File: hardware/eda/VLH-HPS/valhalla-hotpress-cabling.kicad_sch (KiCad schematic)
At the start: 42 parts

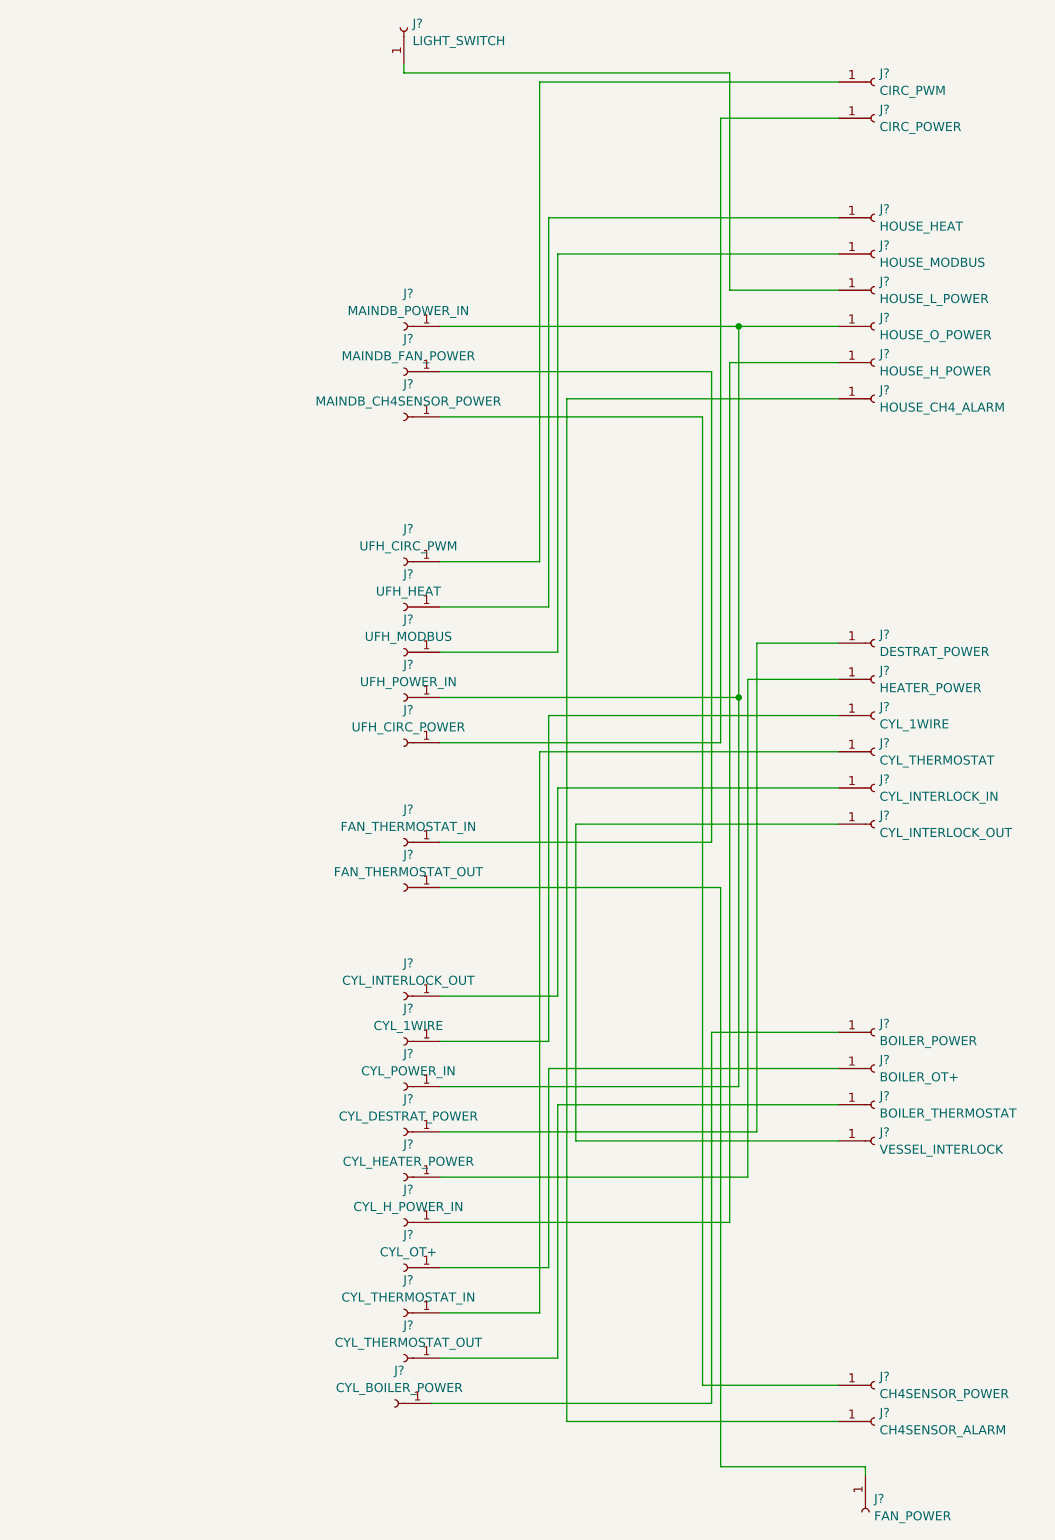
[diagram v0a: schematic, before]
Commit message: UPDATE: refined hotpress cabling plan, solved the fan thermostat 2-in-1 issue.  - upgraded to KiCAD 8 while at it.
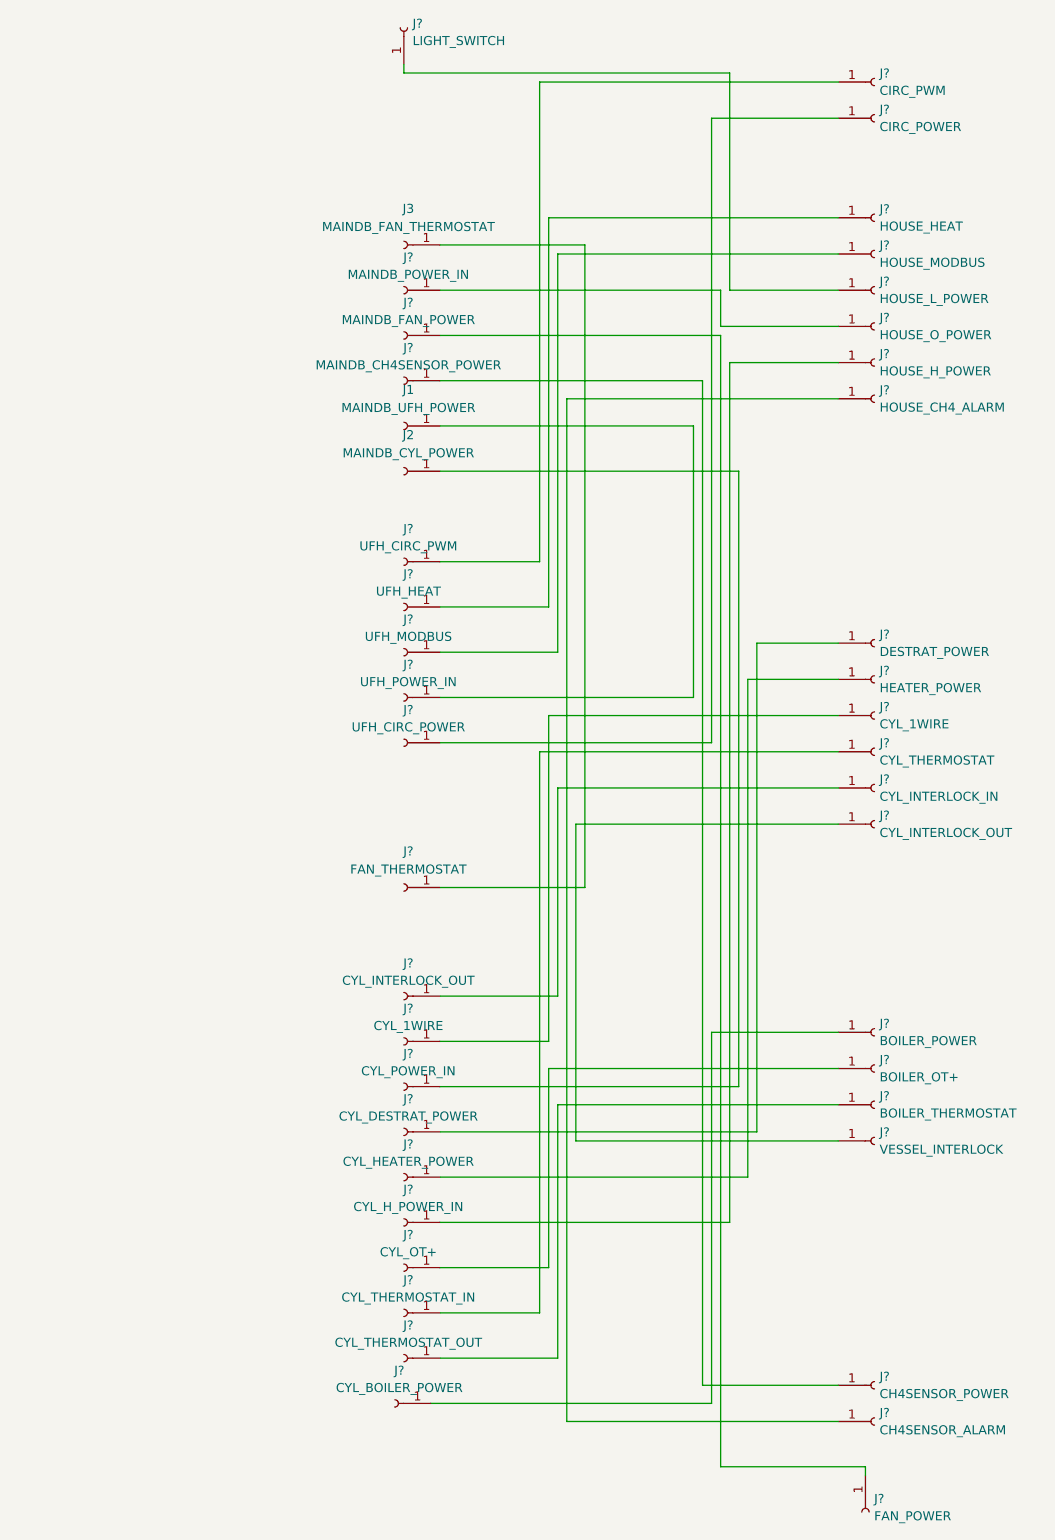
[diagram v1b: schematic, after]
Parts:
- removed J?: FAN_THERMOSTAT_IN, symbol Connector:Conn_01x01_Socket
- added J1: MAINDB_UFH_POWER, symbol Connector:Conn_01x01_Socket
- added J2: MAINDB_CYL_POWER, symbol Connector:Conn_01x01_Socket
- added J3: MAINDB_FAN_THERMOSTAT, symbol Connector:Conn_01x01_Socket
- J?: value FAN_THERMOSTAT_OUT -> FAN_THERMOSTAT
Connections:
- net at J?.1 (Pin_1), J?.1 (Pin_1): no longer J?.1 (Pin_1), J?.1 (Pin_1)
- net at J?.1 (Pin_1): now also J?.1 (Pin_1)
- net at J?.1 (Pin_1): now also J3.1 (Pin_1); no longer J?.1 (Pin_1)
- new net: J2.1 (Pin_1), J?.1 (Pin_1)
- new net: J1.1 (Pin_1), J?.1 (Pin_1)
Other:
- moved on the sheet: J?

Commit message: UPDATE: added CPU cable glands to the hotpress cabling plan.
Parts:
- added J10, J11: CYL_SIGNALS, symbol Connector:Conn_01x01_Socket
- added J4: UFH_CPU_POWER_IN, symbol Connector:Conn_01x01_Socket
- added J5: UFH_CPU_POWER, symbol Connector:Conn_01x01_Socket
- added J6, J7: UFH_SIGNALS, symbol Connector:Conn_01x01_Socket
- added J8: CYL_CPU_POWER_IN, symbol Connector:Conn_01x01_Socket
- added J9: CYL_CPU_POWER, symbol Connector:Conn_01x01_Socket
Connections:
- new net: J10.1 (Pin_1), J11.1 (Pin_1)
- new net: J6.1 (Pin_1), J7.1 (Pin_1)
- new net: J8.1 (Pin_1), J9.1 (Pin_1)
- new net: J4.1 (Pin_1), J5.1 (Pin_1)
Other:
- moved on the sheet: J?
